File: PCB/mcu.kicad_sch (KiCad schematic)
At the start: 6 parts, among them U1 STM32U5A5ZJTxQ, Y1 FOXSDLF/080-20

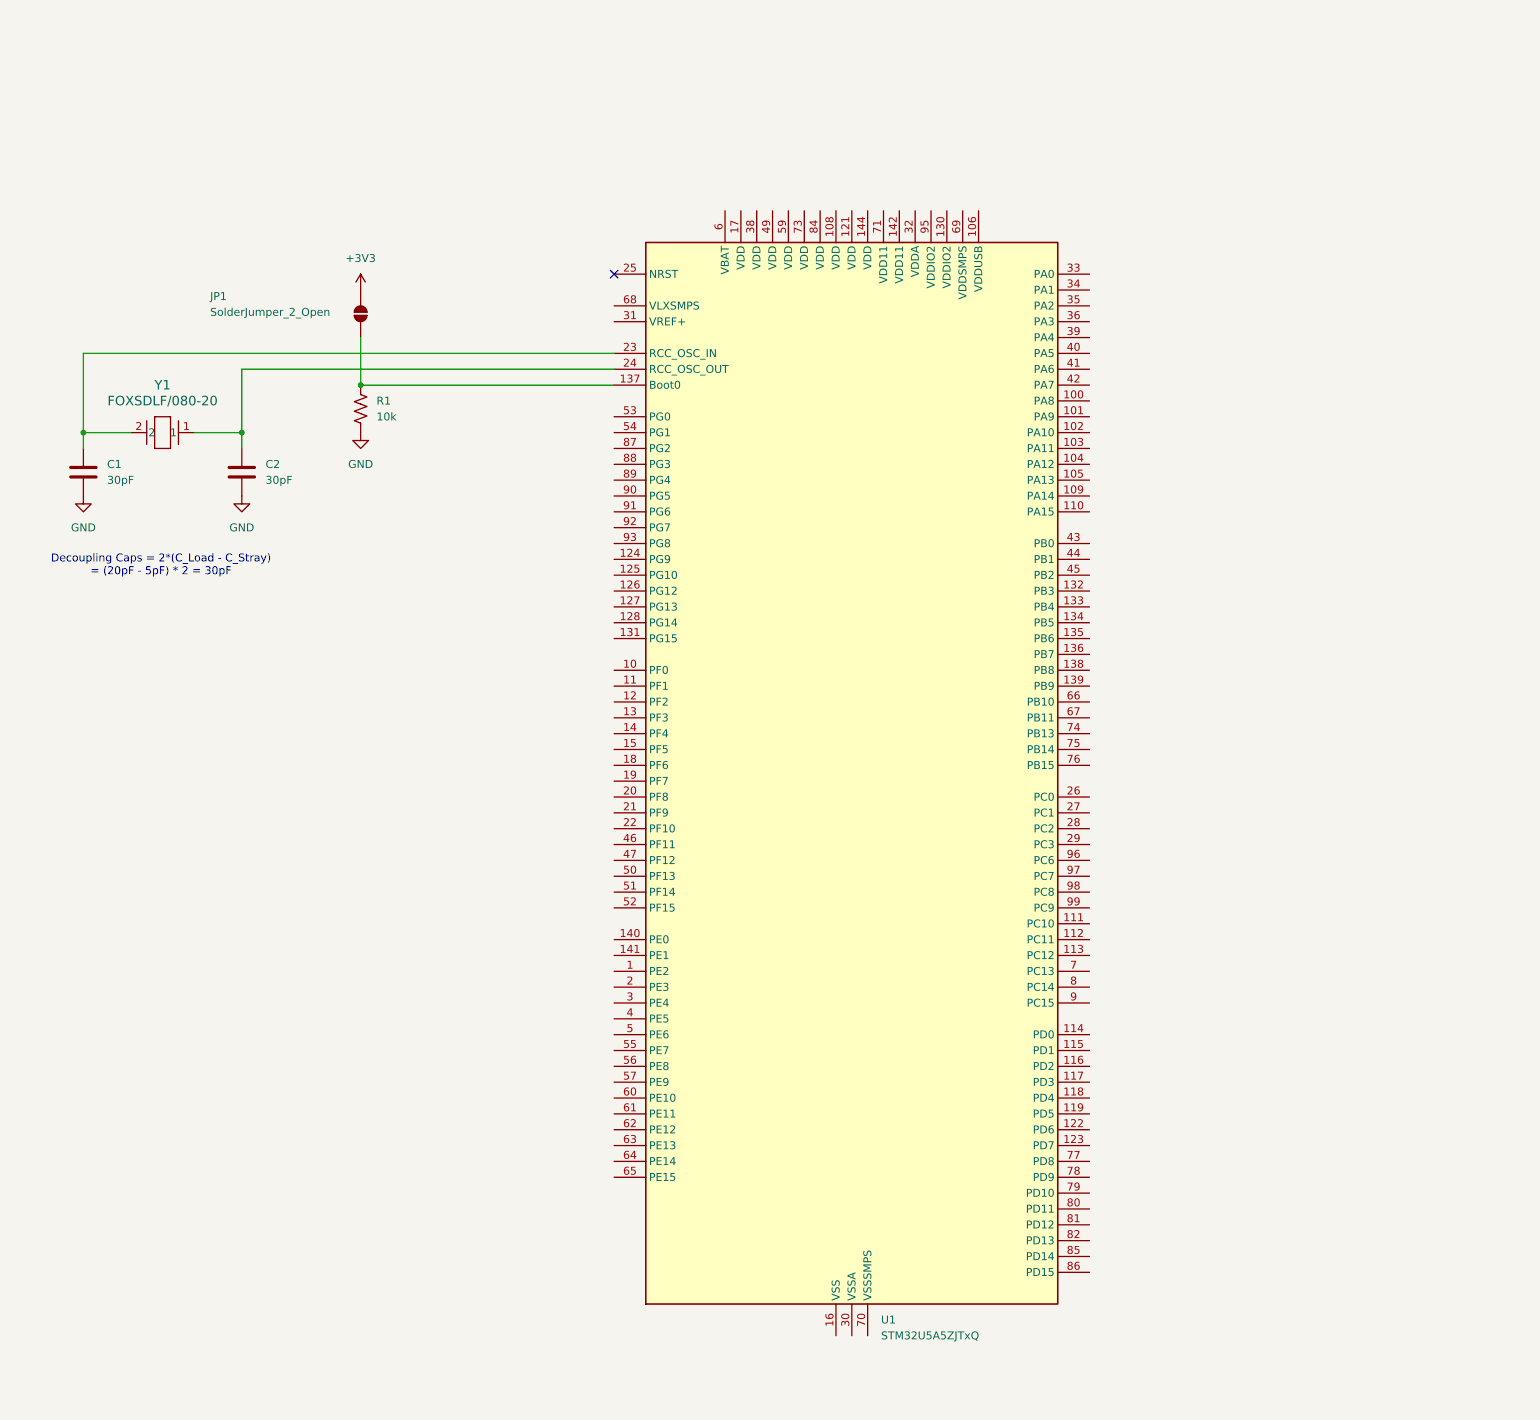
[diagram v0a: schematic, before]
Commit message: Decoupling caps added to schematic
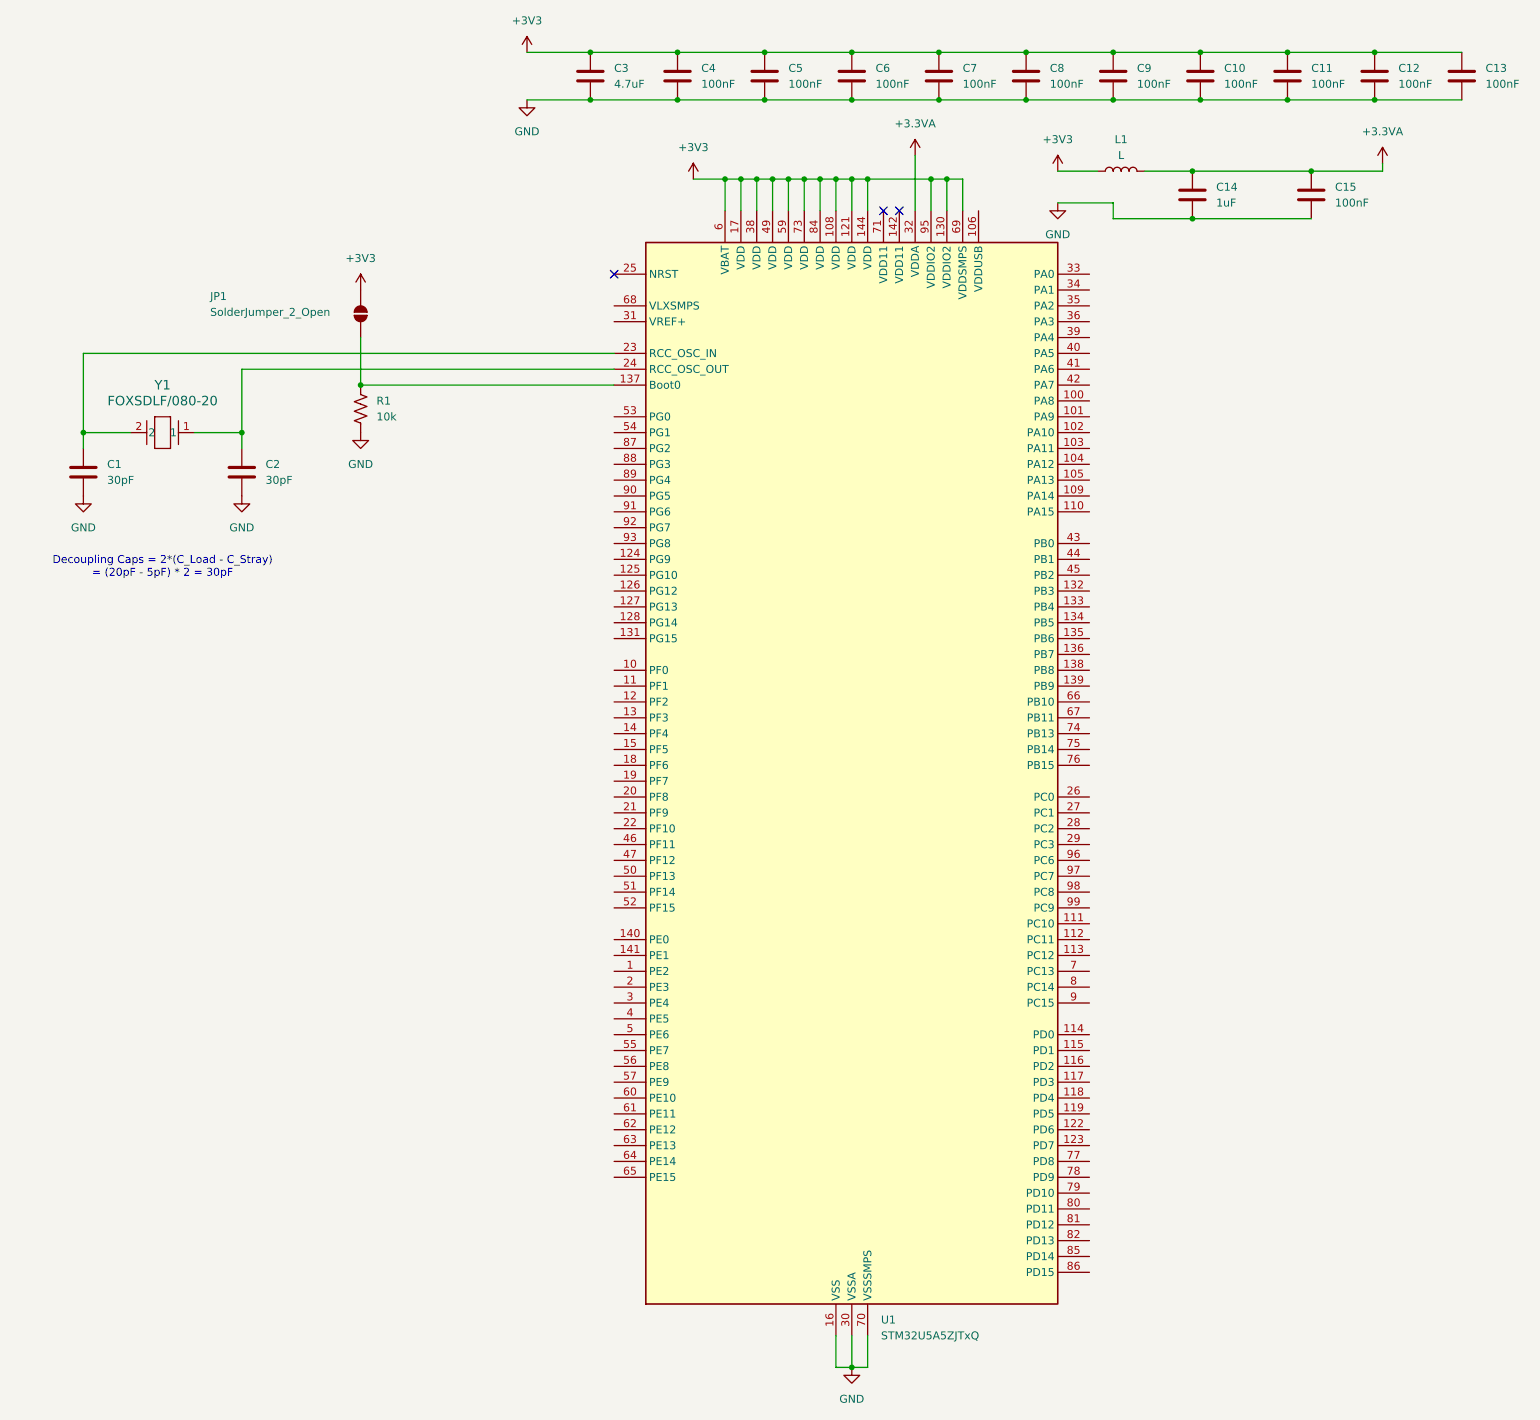
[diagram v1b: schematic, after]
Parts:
- added C10, C11, C12, C13, C15, C4, C5, C6, C7, C8, C9: 100nF, symbol Device:C
- added C14: 1uF, symbol Device:C
- added C3: 4.7uF, symbol Device:C
- added L1: L, symbol Device:L
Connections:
- net +3V3: now also U1.108 (VDD), U1.121 (VDD), U1.130 (VDDIO2), U1.144 (VDD), U1.17 (VDD), U1.38 (VDD), U1.49 (VDD), U1.59 (VDD), U1.6 (VBAT), U1.69 (VDDSMPS), U1.73 (VDD), U1.84 (VDD), U1.95 (VDDIO2), C10.1, C11.1, C12.1, C13.1, C3.1, C4.1, C5.1, C6.1, C7.1, C8.1, C9.1, L1.1
- net GND: now also U1.107 (VSS), U1.120 (VSS), U1.129 (VSS), U1.143 (VSS), U1.16 (VSS), U1.30 (VSSA), U1.37 (VSS), U1.48 (VSS), U1.58 (VSS), U1.70 (VSSSMPS), U1.72 (VSS), U1.83 (VSS), U1.94 (VSS), C10.2, C11.2, C12.2, C13.2, C14.2, C15.2, C3.2, C4.2, C5.2, C6.2, C7.2, C8.2, C9.2
- net +3.3VA: now reaches U1.32 (VDDA)
- net +3.3VA: now also C14.1, C15.1, L1.2
- no-connect marks 1 -> 3

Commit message: Switch from STM32U5A5ZJT6Q to STM32U5A5VJT6Q in PCB and CubeIDE
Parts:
- removed C11, C12, C13: 100nF, symbol Device:C
- removed U1: STM32U5A5ZJTxQ, Package_QFP:LQFP-144_20x20mm_P0.5mm, symbol MCU_ST_STM32U5:STM32U5A5ZJTxQ
- added U1: STM32U5A5VJTxQ, Package_QFP:LQFP-100_14x14mm_P0.5mm, symbol MCU_ST_STM32U5:STM32U5A5VJTxQ
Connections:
- net +3.3VA: now also U1.21 (VDDA)
- net +3V3: now also U1.100 (VDD), U1.11 (VDD), U1.27 (VDD), U1.51 (VDD), U1.6 (VBAT), U1.75 (VDD)
- net at JP1.1 (A), R1.1: now also U1.94 (PH3)
- net at C2.1, Y1.1: now also U1.13 (PH1)
- net at C1.1, Y1.2: now also U1.12 (PH0)
- new net: U1.10 (VSS), U1.26 (VSS), U1.50 (VSS), U1.74 (VSS), U1.99 (VSS)
- no-connect marks 3 -> 4

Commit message: Added LiPo charge IC
uses "power path" so we can run the device even when its being charged. That might be nice for debugging if I can setup debugging over USB in the future
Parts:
- L1: value L -> 27nH
- R1: value 10k -> 100k
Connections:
- net GND: now also U1.10 (VSS), U1.19 (VSSA), U1.26 (VSS), U1.50 (VSS), U1.74 (VSS), U1.99 (VSS)
- net Boot0: now reaches JP1.1 (A), R1.1, U1.94 (PH3)
- net OSC_OUT: now reaches C2.1, U1.13 (PH1), Y1.1
- net OSC_IN: now reaches C1.1, U1.12 (PH0), Y1.2
- net USB_D-: now reaches U1.70 (PA11)
- net USB_D+: now reaches U1.71 (PA12)
- net SWD_IO: now reaches U1.72 (PA13)
- net SWD_CLK: now reaches U1.76 (PA14)
- no-connect marks 4 -> 3
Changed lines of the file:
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@@
 	)
 	(junction
-		(at 207.01 231.14)
+		(at 198.12 186.69)
 		(diameter 0)
 		(color 0 0 0 0)
@@
 		(at 209.55 45.72)
 	)
-	(no_connect
-		(at 168.91 55.88)
-	)
 	(wire
 		(pts
@@
 	(wire
 		(pts
-			(xy 204.47 226.06) (xy 204.47 231.14)
-		)
-		(stroke
-			(width 0)
-			(type default)
-		)
-	)
-	(wire
-		(pts
 			(xy 154.94 20.32) (xy 165.1 20.32)
 		)
@@
 	(wire
 		(pts
-			(xy 207.01 226.06) (xy 207.01 231.14)
-		)
-		(stroke
-			(width 0)
-			(type default)
-		)
-	)
-	(wire
-		(pts
 			(xy 189.23 40.64) (xy 186.69 40.64)
 		)
@@
 	(wire
 		(pts
-			(xy 209.55 226.06) (xy 209.55 231.14)
-		)
-		(stroke
-			(width 0)
-			(type default)
-		)
-	)
-	(wire
-		(pts
 			(xy 207.01 27.94) (xy 220.98 27.94)
 		)
@@
 	(wire
 		(pts
+			(xy 199.39 182.88) (xy 199.39 186.69)
+		)
+		(stroke
+			(width 0)
+			(type default)
+		)
+	)
+	(wire
+		(pts
 			(xy 83.82 81.28) (xy 91.44 81.28)
 		)
@@
 	(wire
 		(pts
-			(xy 204.47 231.14) (xy 207.01 231.14)
-		)
-		(stroke
-			(width 0)
-			(type default)
-		)
-	)
-	(wire
-		(pts
-			(xy 209.55 231.14) (xy 207.01 231.14)
+			(xy 199.39 186.69) (xy 198.12 186.69)
+		)
+		(stroke
+			(width 0)
+			(type default)
+		)
+	)
+	(wire
+		(pts
+			(xy 196.85 186.69) (xy 196.85 182.88)
 		)
 		(stroke
@@
 			(width 0)
 			(type default)
+		)
+	)
+	(wire
+		(pts
+			(xy 196.85 186.69) (xy 198.12 186.69)
+		)
+		(stroke
+			(width 0)
+			(type default)
+		)
+	)
+	(label "Boot0"
+		(at 156.21 73.66 0)
+		(effects
+			(font
+				(size 1.27 1.27)
+			)
+			(justify left bottom)
+		)
+	)
+	(label "OSC_IN"
+		(at 156.21 68.58 0)
+		(effects
+			(font
+				(size 1.27 1.27)
+			)
+			(justify left bottom)
+		)
+	)
+	(label "OSC_OUT"
+		(at 156.21 71.12 0)
+		(effects
+			(font
+				(size 1.27 1.27)
+			)
+			(justify left bottom)
+		)
+	)
+	(hierarchical_label "SWD_IO"
+		(shape input)
+		(at 229.87 88.9 0)
+		(effects
+			(font
+				(size 1.27 1.27)
+			)
+			(justify left)
+		)
+	)
+	(hierarchical_label "USB_D+"
+		(shape input)
+		(at 229.87 86.36 0)
+		(effects
+			(font
+				(size 1.27 1.27)
+			)
+			(justify left)
+		)
+	)
+	(hierarchical_label "USB_D-"
+		(shape input)
+		(at 229.87 83.82 0)
+		(effects
+			(font
+				(size 1.27 1.27)
+			)
+			(justify left)
+		)
+	)
+	(hierarchical_label "SWD_CLK"
+		(shape input)
+		(at 229.87 91.44 0)
+		(effects
+			(font
+				(size 1.27 1.27)
+			)
+			(justify left)
 		)
 	)
@@
 	(symbol
 		(lib_id "power:GND")
-		(at 207.01 231.14 0)
+		(at 198.12 186.69 0)
 		(unit 1)
 		(exclude_from_sim no)
@@
 		(fields_autoplaced yes)
 		(property "Reference" "#PWR06"
-			(at 207.01 237.49 0)
+			(at 198.12 193.04 0)
 			(effects
 				(font
@@
 		)
 		(property "Value" "GND"
-			(at 207.01 236.22 0)
+			(at 198.12 191.77 0)
 			(effects
 				(font
@@
 		)
 		(property "Footprint" ""
-			(at 207.01 231.14 0)
+			(at 198.12 186.69 0)
 			(effects
 				(font
@@
 		)
 		(property "Datasheet" ""
-			(at 207.01 231.14 0)
+			(at 198.12 186.69 0)
 			(effects
 				(font
@@
 		)
 		(property "Description" "Power symbol creates a global label with name \"GND\" , ground"
-			(at 207.01 231.14 0)
+			(at 198.12 186.69 0)
 			(effects
 				(font
@@
 			)
 		)
-		(property "Value" "10k"
+		(property "Value" "100k"
 			(at 130.81 78.7399 0)
 			(effects
@@
 		)
 		(pin "94"
-			(alternate "Boo0")
+			(alternate "Boot0")
 		)
 		(pin "46"
@@
 			)
 		)
-		(property "Value" "L"
+		(property "Value" "27nH"
 			(at 250.19 36.83 90)
 			(effects
